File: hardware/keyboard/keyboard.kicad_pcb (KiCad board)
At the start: 2 copper layers, 80.3 x 73.7 mm, 24 parts, among them J1 Conn_01x06, SW1 SW_PUSH, SW2 SW_PUSH, SW3 SW_PUSH, SW4 SW_PUSH, SW5 SW_PUSH, SW6 SW_PUSH, SW7 SW_PUSH, SW8 SW_PUSH, SW9 SW_PUSH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

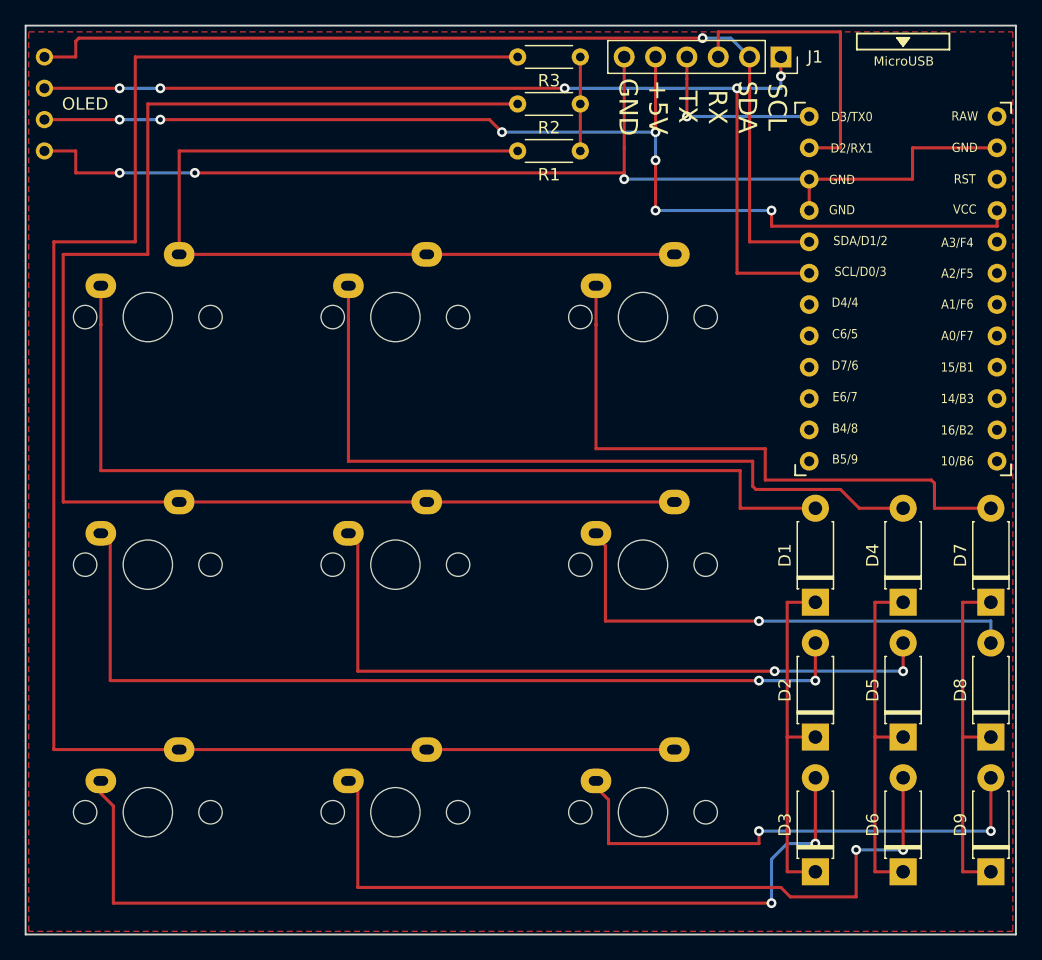
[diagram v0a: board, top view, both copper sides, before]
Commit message: Fixed broken connections in hierarchy
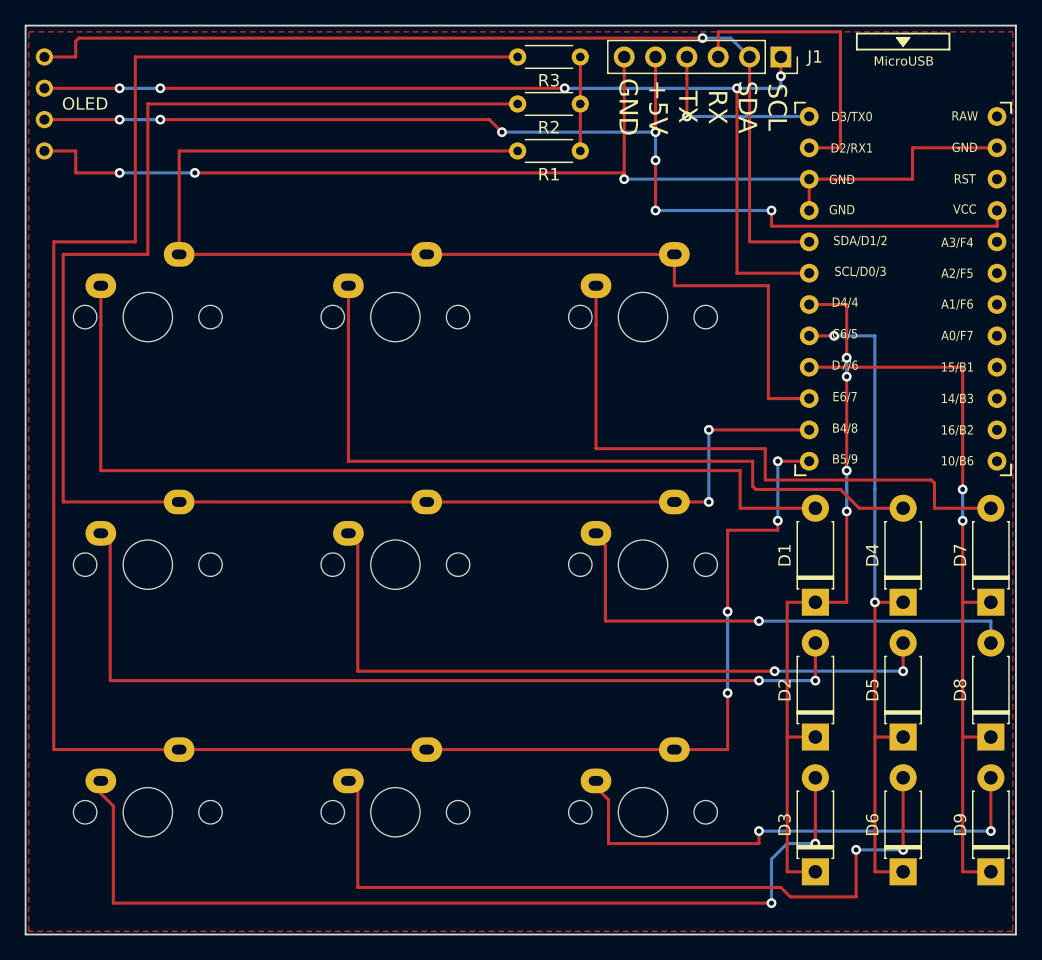
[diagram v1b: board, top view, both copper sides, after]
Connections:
- R1 pad 1: /KeyMatrix/PWR -> +5V
- R2 pad 1: /KeyMatrix/PWR -> +5V
- R3 pad 1: /KeyMatrix/PWR -> +5V
- U1 pad 10: /ROW1 -> /KeyMatrix/ROW1
- U1 pad 11: /ROW2 -> /KeyMatrix/ROW2
- U1 pad 12: /ROW3 -> /KeyMatrix/ROW3
- U1 pad 7: /COL1 -> /KeyMatrix/COL1
- U1 pad 8: /COL2 -> /KeyMatrix/COL2
- U1 pad 9: /COL3 -> /KeyMatrix/COL3
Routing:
- net /KeyMatrix/ROW3: track 144.0 -> 178.3 mm, vias 0 -> 4
- net /KeyMatrix/COL3: track 28.7 -> 60.2 mm, vias 0 -> 2
- net /KeyMatrix/COL1: track 28.7 -> 58.4 mm, vias 0 -> 4
- net /KeyMatrix/COL2: track 28.7 -> 55.6 mm, vias 0 -> 2
- net /KeyMatrix/ROW1: track 75.9 -> 98.6 mm
- net /KeyMatrix/ROW2: track 118.6 -> 135.4 mm, vias 0 -> 2
- net +5V: track 92.6 -> 101.8 mm
- net /KeyMatrix/PWR: track 7.62 -> 0.00 mm
